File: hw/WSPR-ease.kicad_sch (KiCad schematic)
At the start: 53 parts, among them J101 SMA, J102 SMA, J1301 pwr+data, Q101 MMBF170, U101 GNSS module, U102 ESP32-S3-WROOM-1-N8R8, U103 TPS22918DBVR, U104 TPS74612PQWDRBRQ1, U105 SRV05-4, U106 LMR51430YDDCR

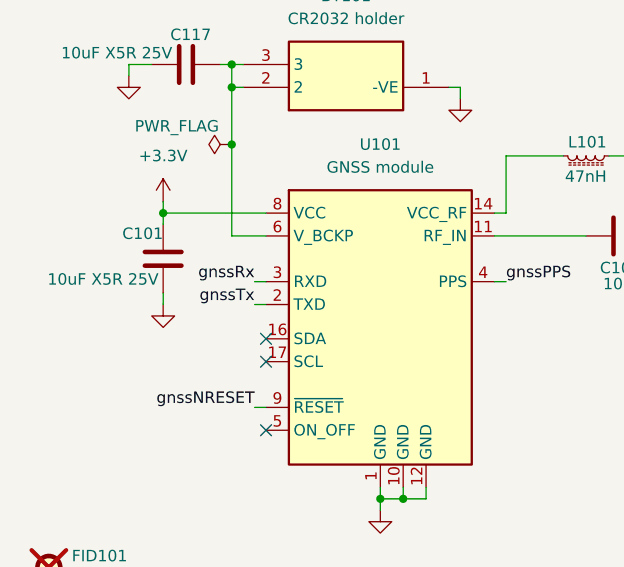
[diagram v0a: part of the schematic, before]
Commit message: Oops. Rx and Tx need to be swapped on GNSS
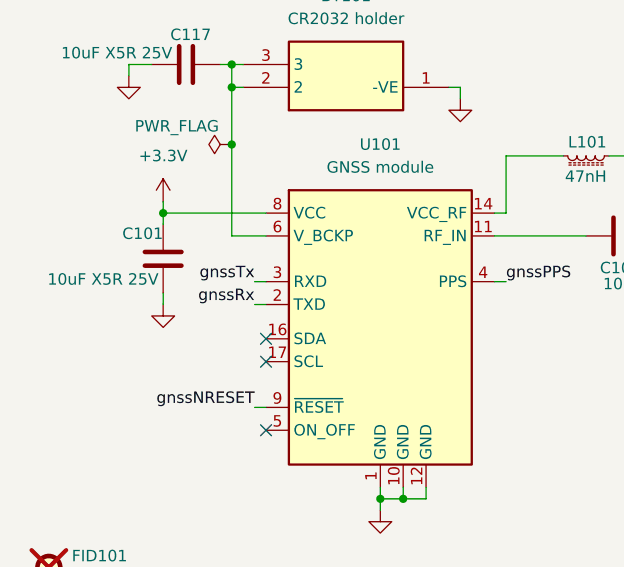
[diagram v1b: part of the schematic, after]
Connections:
- net gnssRx: now also U101.2 (TXD); no longer U101.3 (RXD)
- net gnssTx: now also U101.3 (RXD); no longer U101.2 (TXD)
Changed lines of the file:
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@@
 	)
 	(label "gnssRx"
-		(at 38.1 147.32 180)
+		(at 38.1 149.86 180)
 		(effects
 			(font
@@
 	)
 	(label "gnssTx"
-		(at 38.1 149.86 180)
-		(effects
-			(font
+		(at 38.1 147.32 180)
+		(effects
+			(font

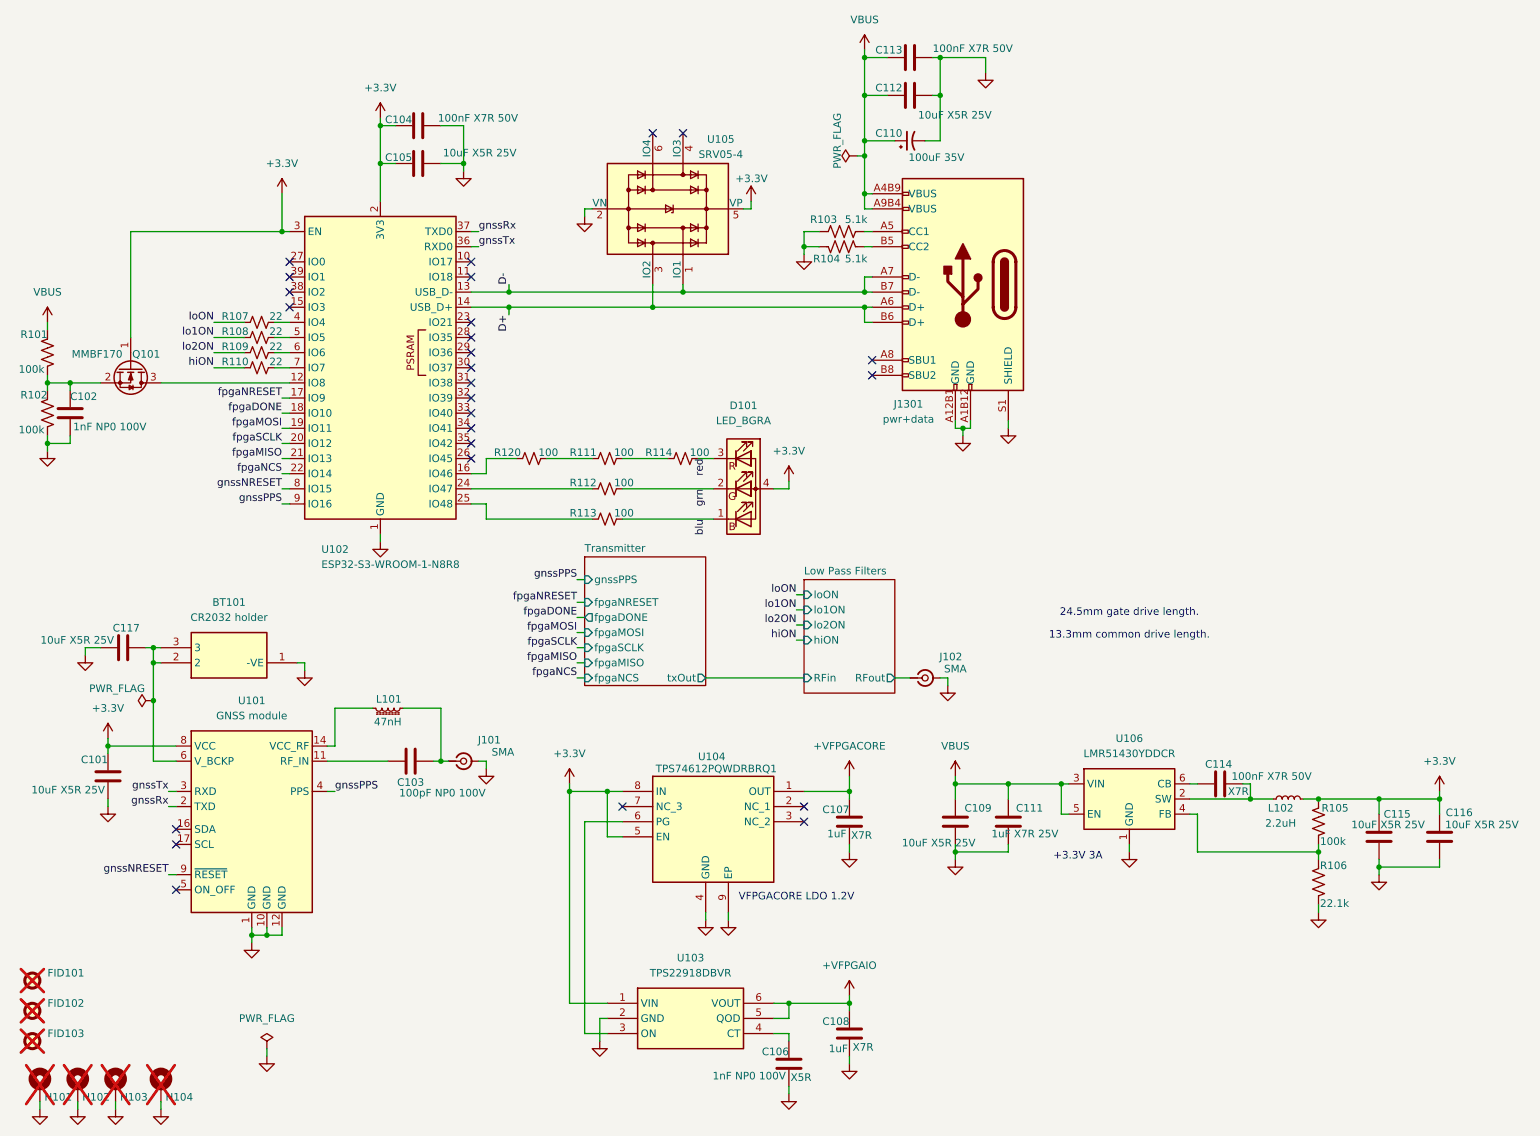
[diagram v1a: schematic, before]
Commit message: Fixed reversed rx/tx on GNSS chip. Solved all ERC and DRC issues
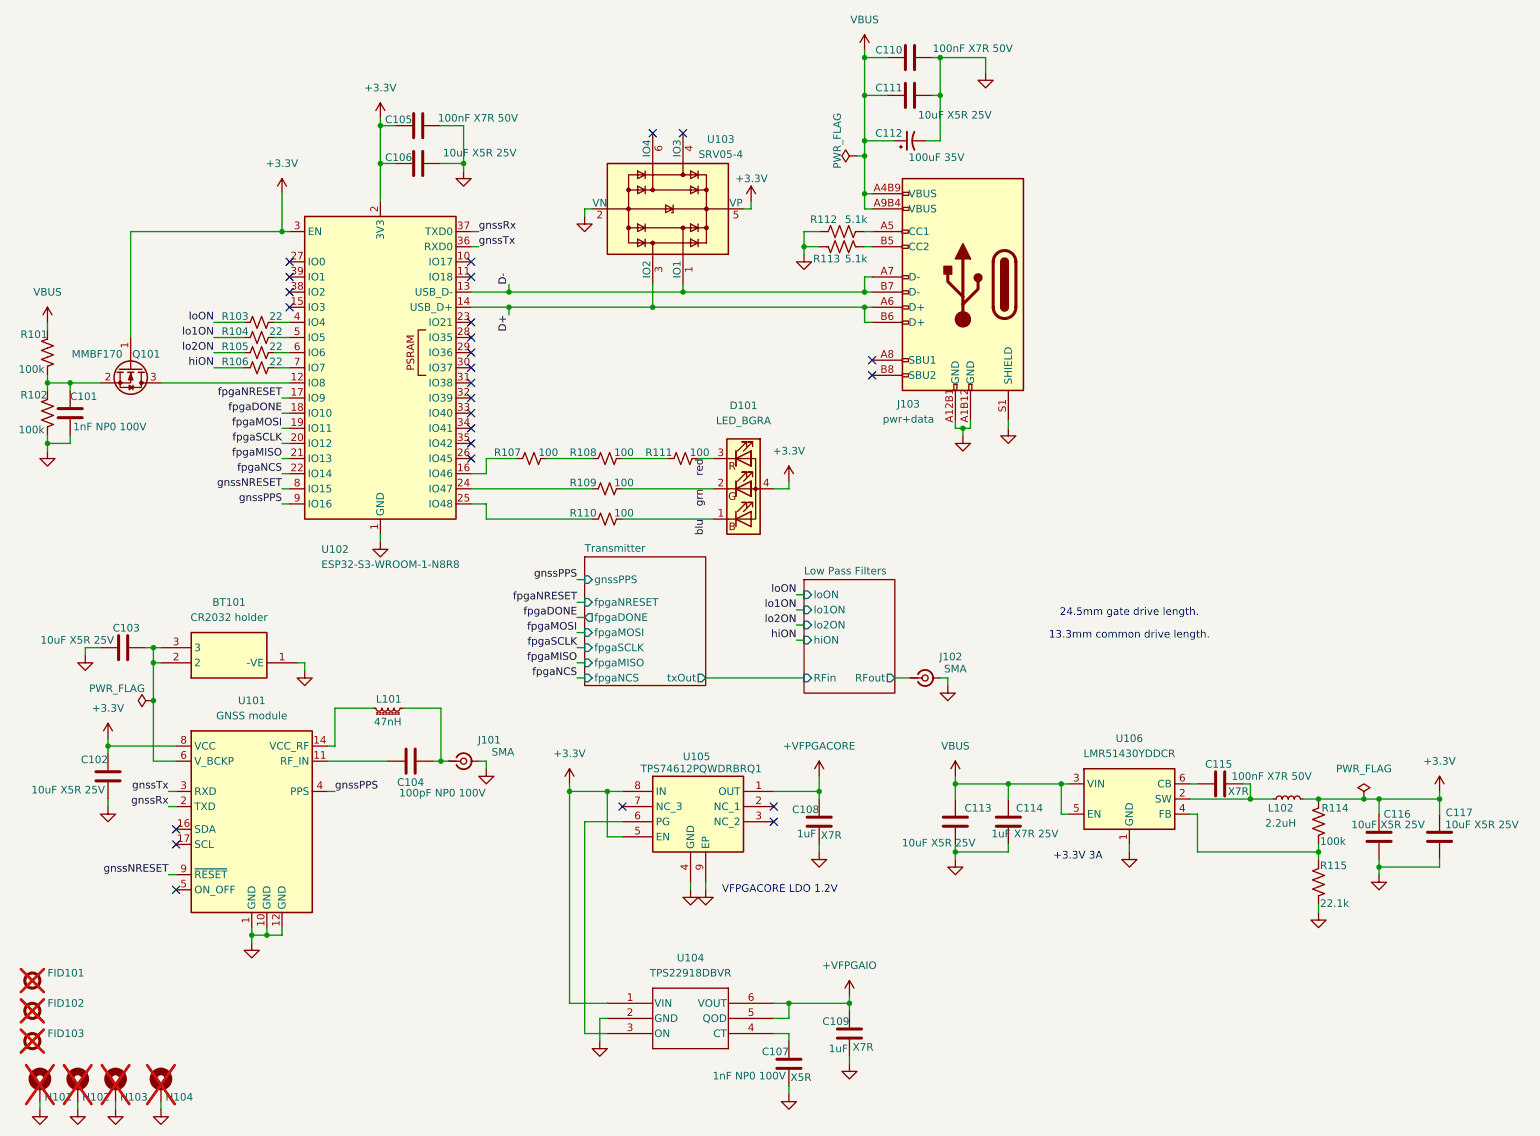
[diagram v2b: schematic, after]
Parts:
- U104: renamed from U103; footprint Package_TO_SOT_SMD:SOT-23-6 -> Library:DBV6_TEX
- U105: renamed from U104; Manufacturer_Name (none) -> Texas Instruments; Manufacturer_Part_Number (none) -> TPS74612PQWDRBRQ1; Mouser Part Number (none) -> 595-PS74612PQWDRBRQ1
- renumbered C102 to C101, C101 to C102, C117 to C103, C103 to C104, C104 to C105, C105 to C106, C106 to C107, C107 to C108, C108 to C109, C113 to C110, C112 to C111, C110 to C112, C109 to C113, C111 to C114, C114 to C115, C115 to C116, C116 to C117, J1301 to J103, R107 to R103, R108 to R104, R109 to R105, R110 to R106, R120 to R107, R111 to R108, R112 to R109, R113 to R110, R114 to R111, R103 to R112, R104 to R113, R105 to R114, R106 to R115, U105 to U103
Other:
- moved on the sheet: C108, U105

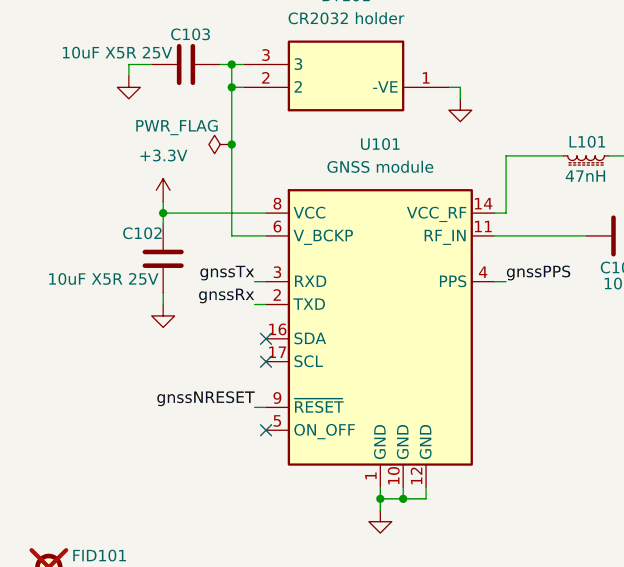
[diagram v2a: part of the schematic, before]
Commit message: Implement real GNSS hardware integration with reset pulse and UART0 migration
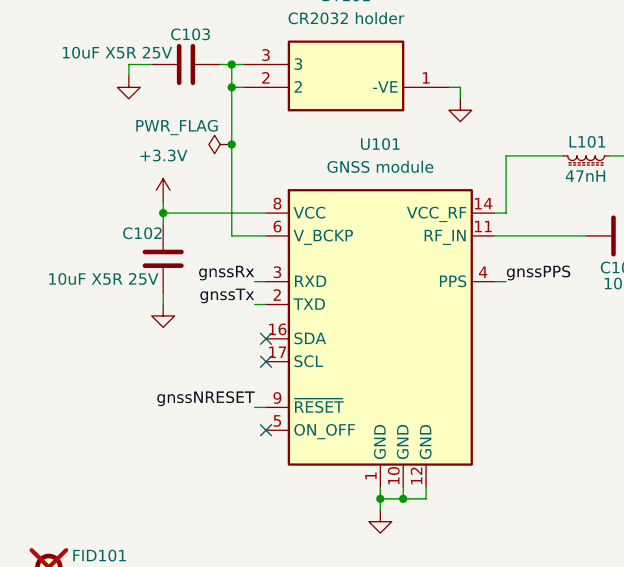
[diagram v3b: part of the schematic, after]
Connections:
- net gnssRx: now also U101.3 (RXD); no longer U101.2 (TXD)
- net gnssTx: now also U101.2 (TXD); no longer U101.3 (RXD)
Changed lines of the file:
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@@
 	)
 	(label "gnssRx"
-		(at 38.1 149.86 180)
+		(at 38.1 147.32 180)
 		(effects
 			(font
@@
 	)
 	(label "gnssTx"
-		(at 38.1 147.32 180)
-		(effects
-			(font
+		(at 38.1 149.86 180)
+		(effects
+			(font

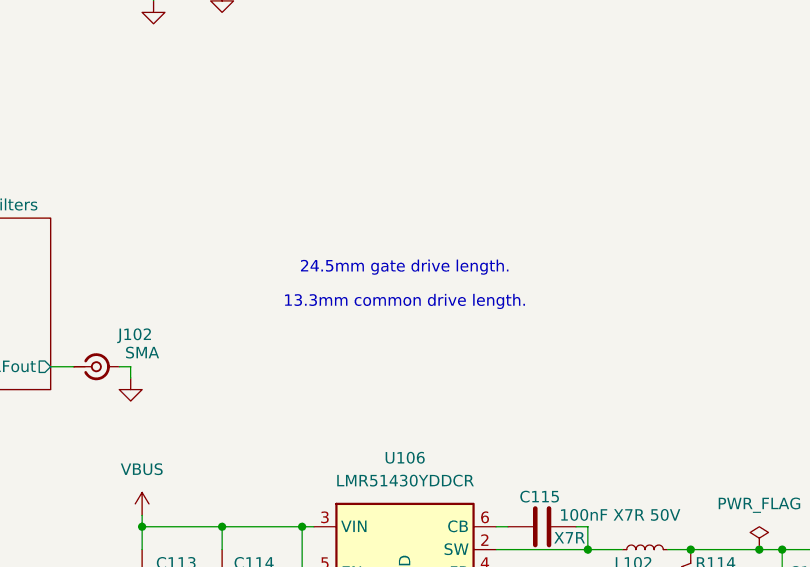
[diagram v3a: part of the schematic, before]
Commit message: Functional but without FPGA loading working well yet
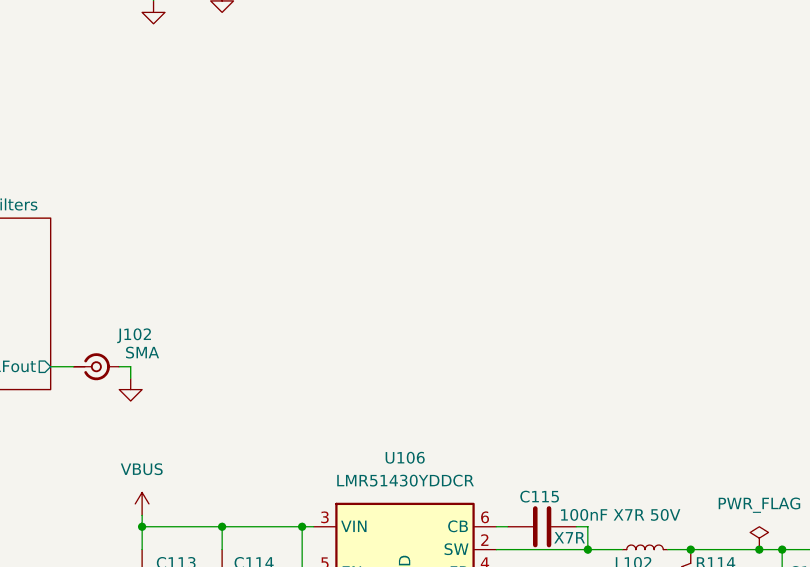
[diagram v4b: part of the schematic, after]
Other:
- note removed: "13.3mm common drive length."
- note removed: "24.5mm gate drive length."
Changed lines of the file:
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@@
 		(company "WB7NAB")
-	)
-	(text "13.3mm common drive length."
-		(exclude_from_sim no)
-		(at 199.39 121.158 0)
-		(effects
-			(font
-				(size 1.27 1.27)
-			)
-		)
 	)
 	(text "VFPGACORE LDO 1.2V"
@@
 		(effects
 			(font
-				(size 1.27 1.27)
-			)
-		)
-	)
-	(text "24.5mm gate drive length."
-		(exclude_from_sim no)
-		(at 199.39 117.348 0)
-		(effects
-			(font

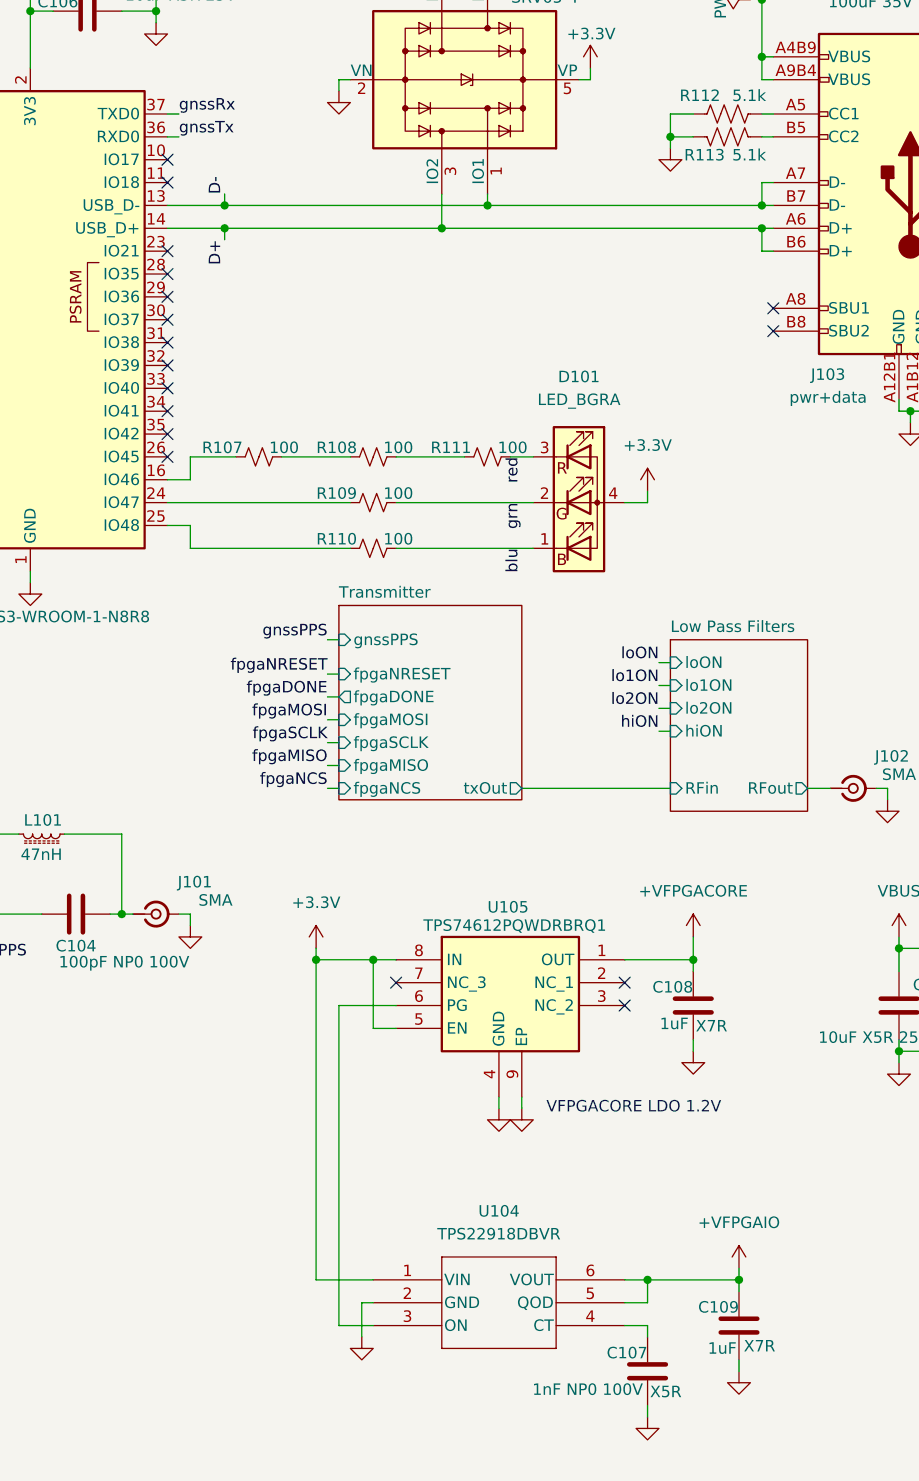
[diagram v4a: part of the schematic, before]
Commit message: Still working on FPGA config loading. Problem is now CMOS lockup caused by FPGACORE vs FPGAIO rails. I moved FPGAIO enable to IO42 on ESP32 and pgFPGACORE to IO41.
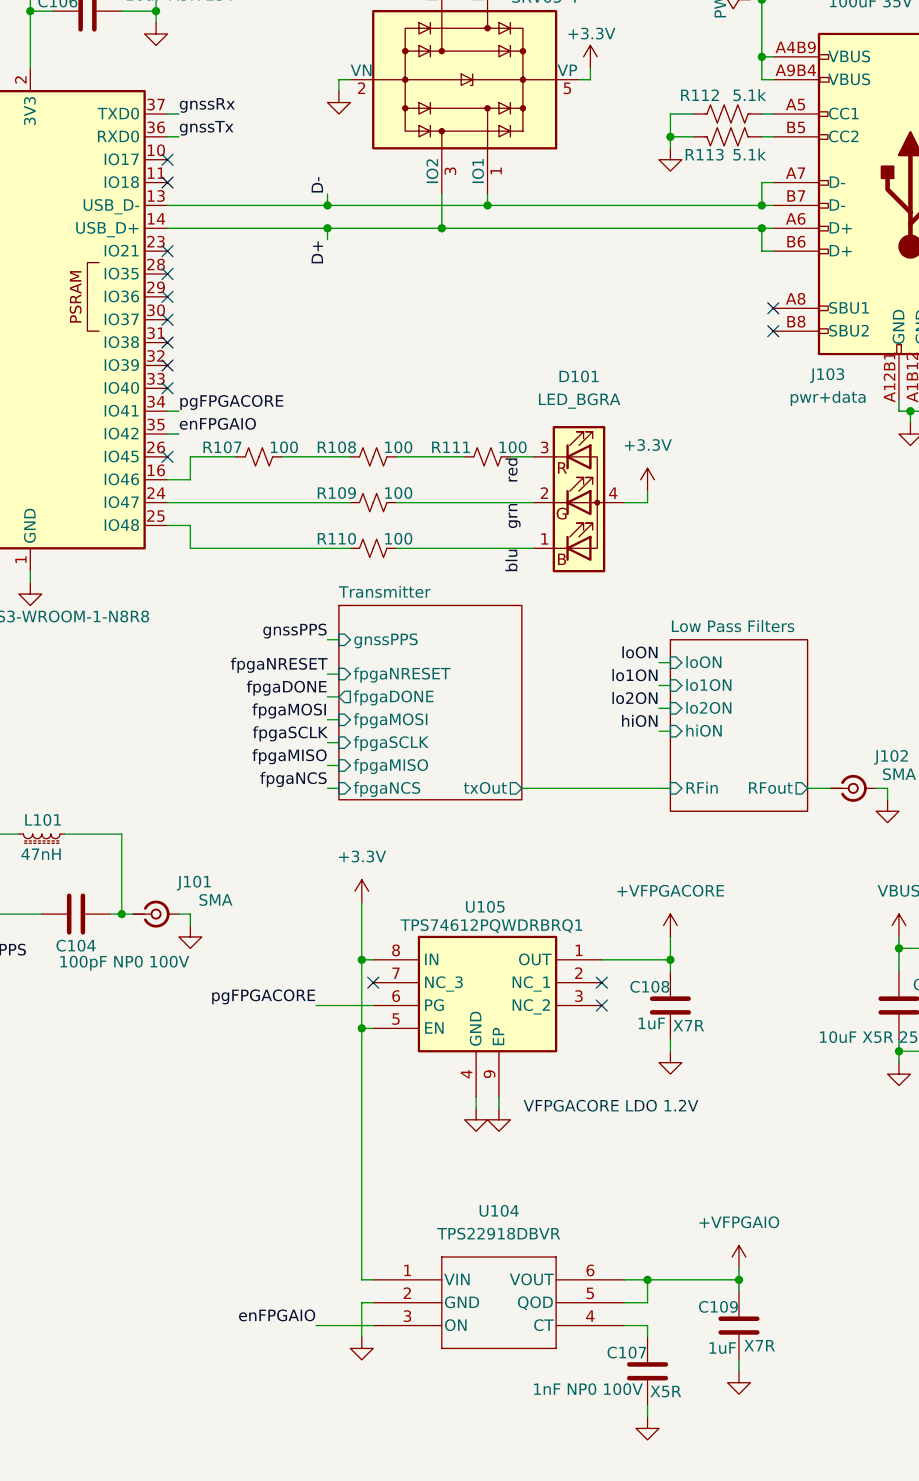
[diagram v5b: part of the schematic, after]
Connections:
- net enFPGAIO: now reaches U104.3 (ON)
- net enFPGAIO: now also U102.35 (IO42); no longer U105.6 (PG)
- net pgFPGACORE: now reaches U102.34 (IO41)
- net pgFPGACORE: now also U105.6 (PG)
- no-connect marks 26 -> 24
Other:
- moved on the sheet: C108, U105
